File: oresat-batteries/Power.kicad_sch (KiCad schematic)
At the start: 88 parts, among them J2 FTS-102-01-X-SJ, U3 MIC842LYC5, U5 LTC3624-3.3, U6 TS5A21366DCUR

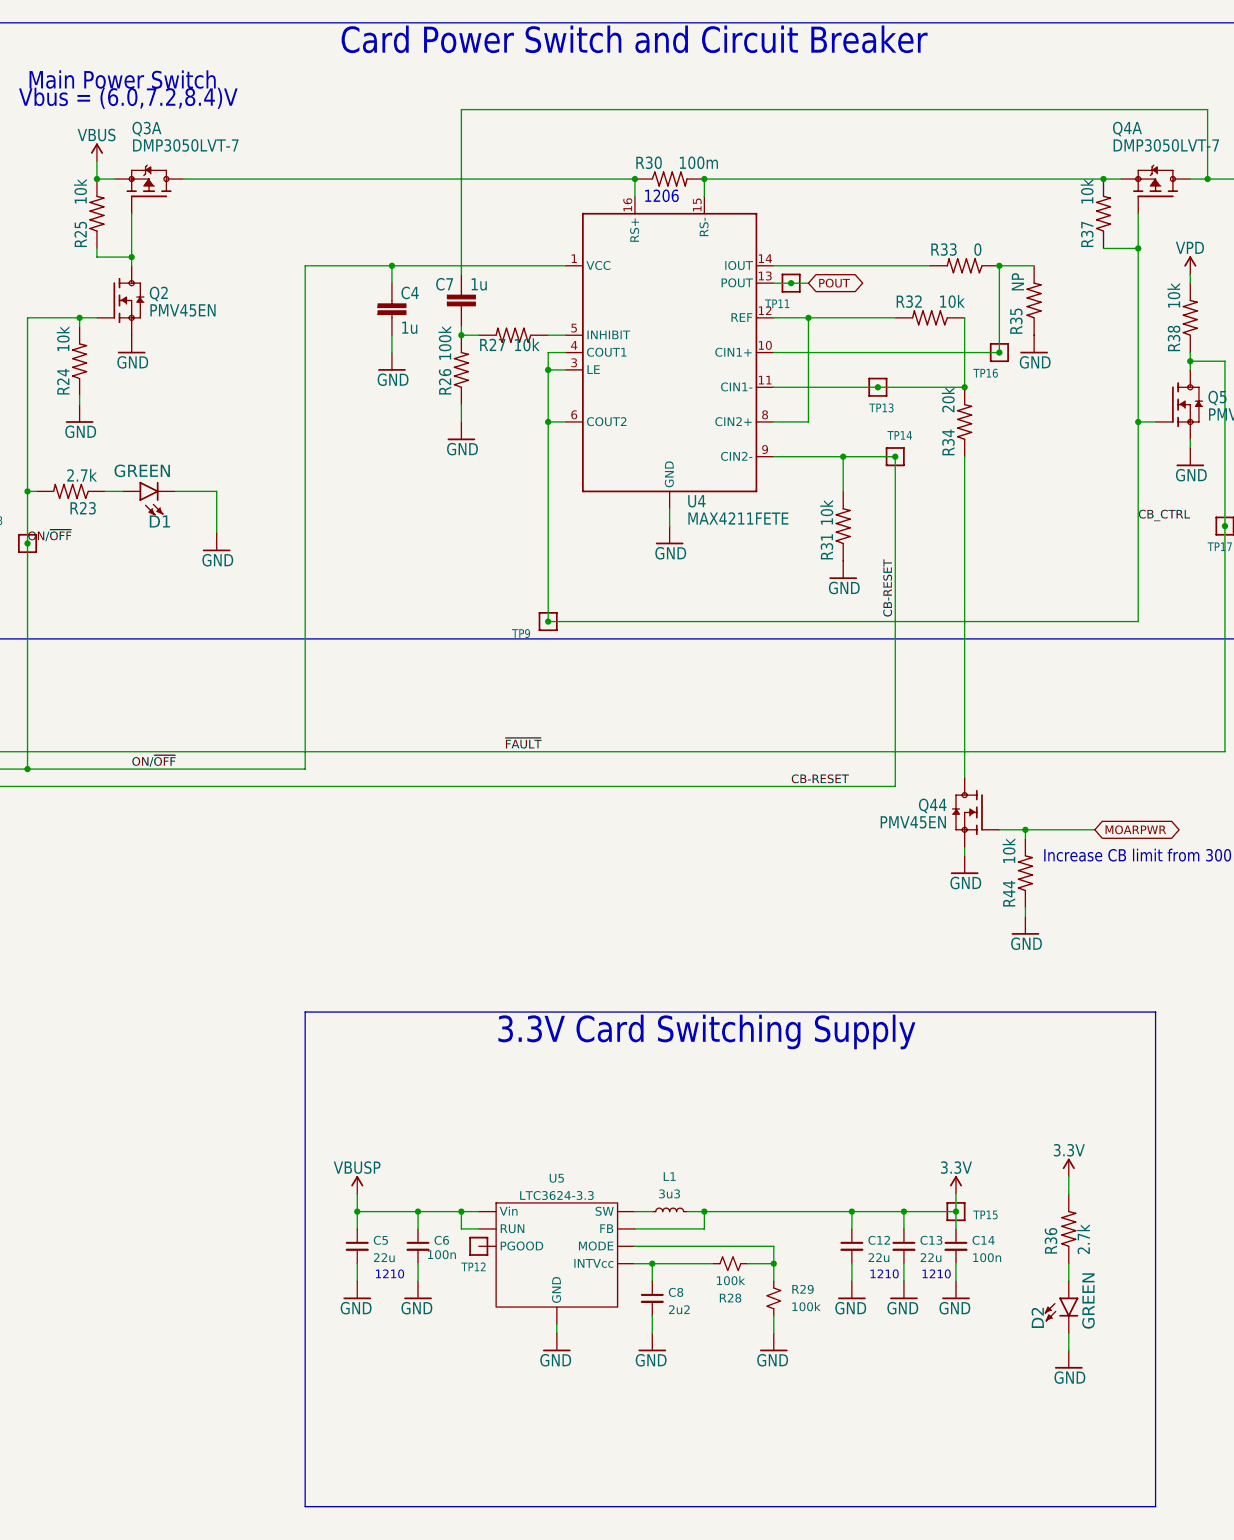
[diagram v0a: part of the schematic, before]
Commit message: Fixed the voltage regulator problem, and the DRC is happy
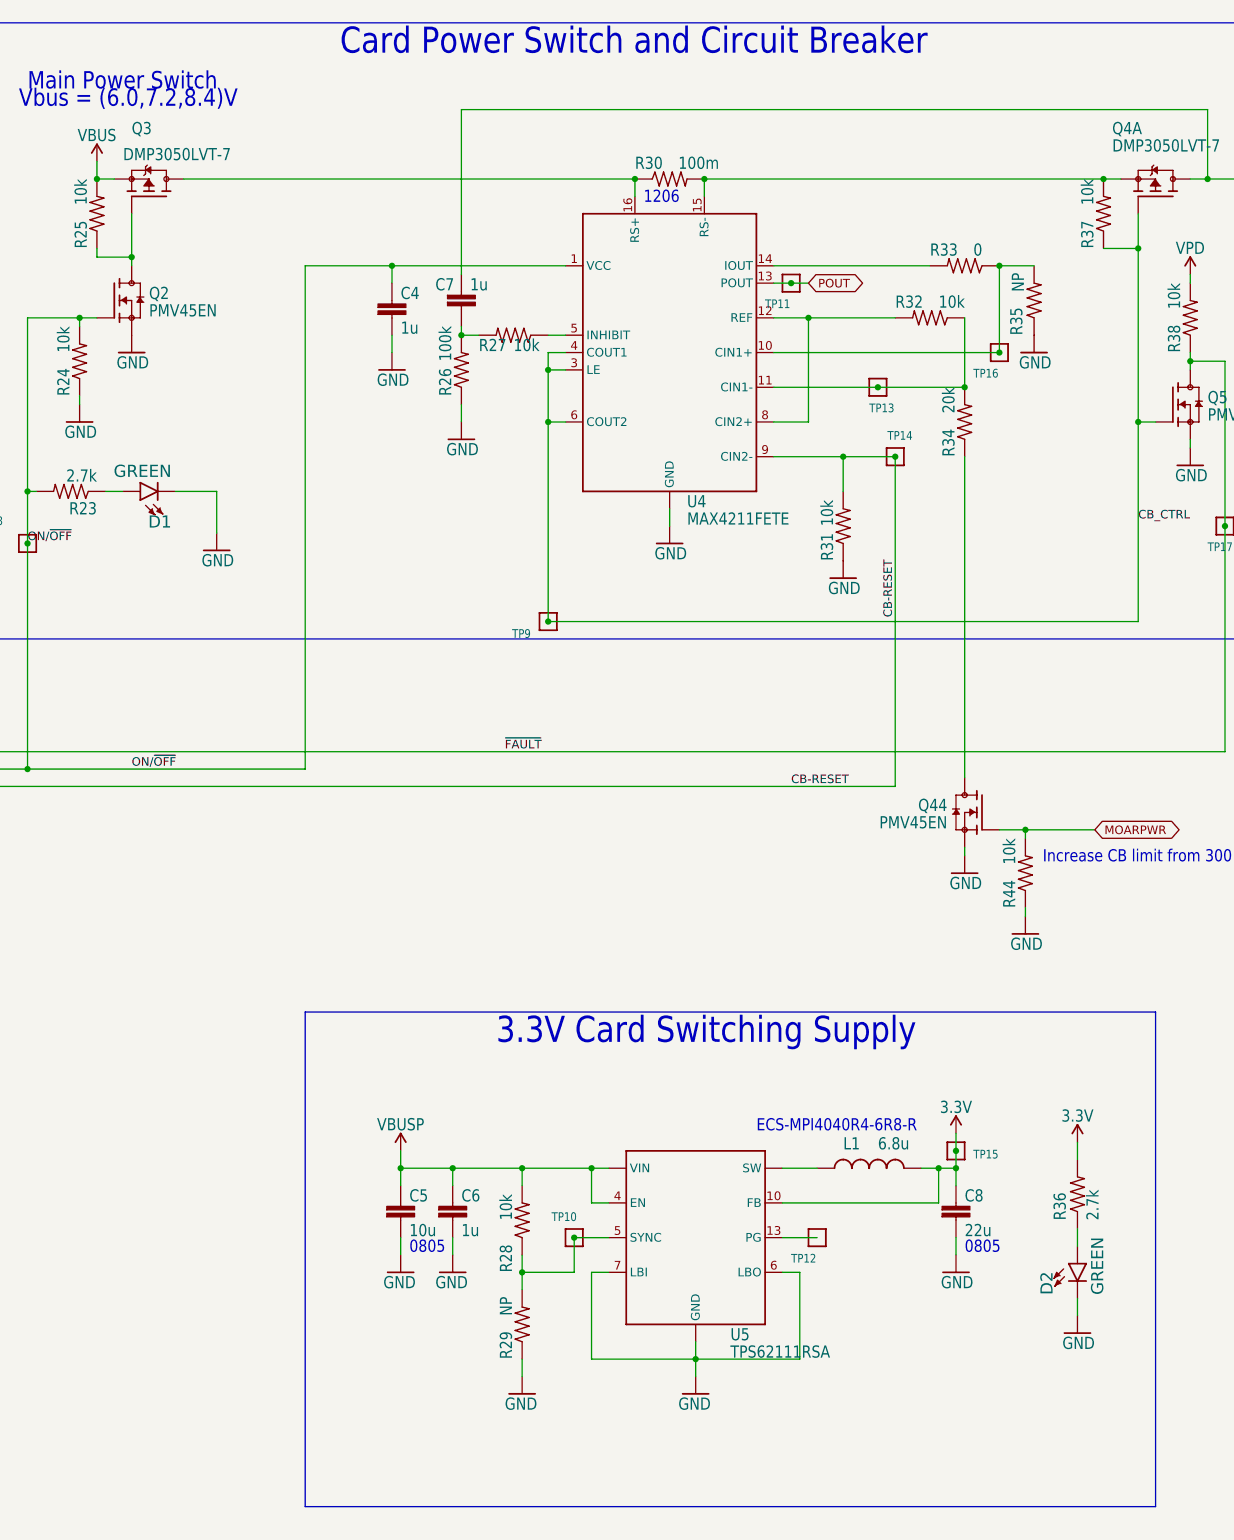
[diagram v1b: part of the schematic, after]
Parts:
- removed C12, C13, C5: 22u, Capacitor_SMD:C_1210_3225Metric, symbol Device:C_Small
- removed C14, C6: 100n, oresat-footprints:0603-SMALL, symbol Device:C_Small
- removed C8: 2u2, oresat-footprints:0603-SMALL, symbol Device:C_Small
- removed L1: 3u3, oresat-footprints:L_ECS-MPI4040, symbol Device:L_Small
- removed R28, R29: 100k, oresat-footprints:0603-SMALL, symbol Device:R_Small_US
- removed U5: LTC3624-3.3, oresat-footprints:DFN-8-1EP_3x3mm_P0.5mm_EP1.65x2.38mm_ThermalVias0.3mm, symbol U-Linear Tech-LTC3624:LTC3624
- added C5, C8: (no value), Capacitor_SMD:C_0805_2012Metric, symbol oresat-batteries-eagle-import:C-EU0805-B-NOSILK
- added C6: (no value), oresat-footprints:0603-SMALL, symbol oresat-batteries-eagle-import:C-EU0603-C-NOSILK
- added L1: (no value), oresat-footprints:L-ECS-MPI4040, symbol oresat-batteries-eagle-import:L-ECS-MPI4040
- added R28, R29: (no value), oresat-footprints:0603-SMALL, symbol oresat-batteries-eagle-import:R-US_0603-C-NOSILK
- added TP10: TEST-POINT-LARGE-SQUARE, oresat-footprints:TestPoint_Pad_1.0x1.0mm, symbol oresat-batteries-eagle-import:TEST-POINT-LARGE-SQUARE
- added U5: (no value), oresat-footprints:U-S-PVQFN-16, symbol oresat-batteries-eagle-import:TPS6211X
- D1, D2, D3: footprint oresat-batteries:LED-0603 -> oresat-footprints:LED-0603
- Q3: value (none) -> DMP3050LVT-7; symbol OreSat-q-mosfet-DMP3050LVT-7-pch-sot23-6:MOSFET-PCH-SOT23-6 -> OreSat-q-mosfet-DMP3050LVT-7-pch-sot23-6:DMP3050LVT-7
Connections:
- net 3.3V: now also C8.1, L1.2, U5.10 (FB)
- net GND: now also C5.2, C6.2, C8.2, R29.1, U5.1 (GND), U5.11 (GND), U5.12 (GND), U5.16 (GND), U5.6 (LBO), U5.7 (LBI), U5.9 (GND), U5.PAD (GND)
- net VBUSP: now also C5.1, C6.1, R28.2, U5.2 (VIN), U5.3 (VIN), U5.4 (EN), U5.8 (VIN)
- net at TP12.1: now also U5.13 (PG)
- new net: R28.1, R29.2, TP10.1, U5.5 (SYNC)
- new net: L1.1, U5.14 (SW), U5.15 (SW)
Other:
- note added: "0805"
- note added: "ECS-MPI4040R4-6R8-R"
- note removed: "1210"
